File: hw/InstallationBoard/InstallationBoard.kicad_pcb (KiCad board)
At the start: 2 copper layers, 79.5 x 44.9 mm, 24 parts, among them J1 +5V, J10 D4, J11 BRIGHT, J15 GND, J16 GND, J2 GND, J3 CLK, J4 SMS, J5 DW, J6 CL2, J7 D1, J8 D2, J9 D3

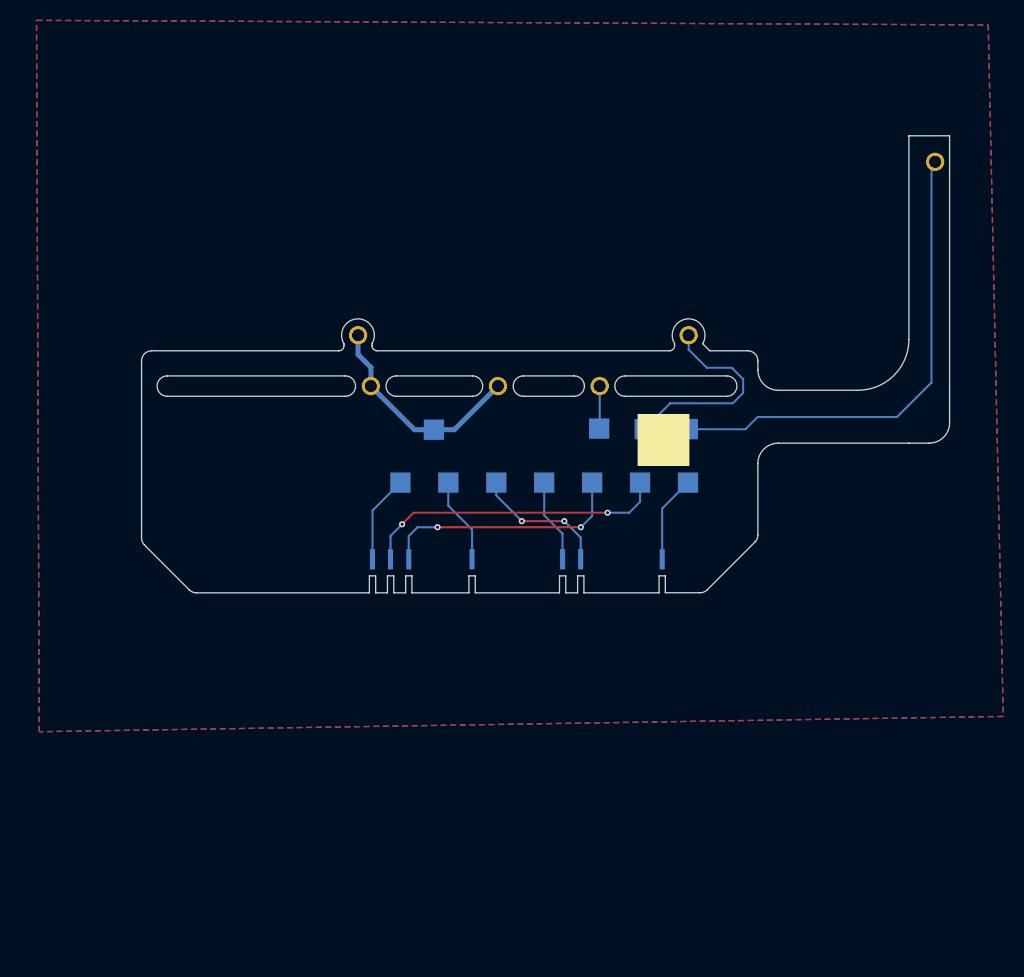
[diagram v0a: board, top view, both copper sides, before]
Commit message: Updated pin assignments on main PCB to match pico code using the correct sequential pins.
54PinTo60RibbonAdapterBoard tweaked trace layout to reduce overall board size slightly.
Added InstallationFlexWithSolderPoints for installing without a ribbon connector.
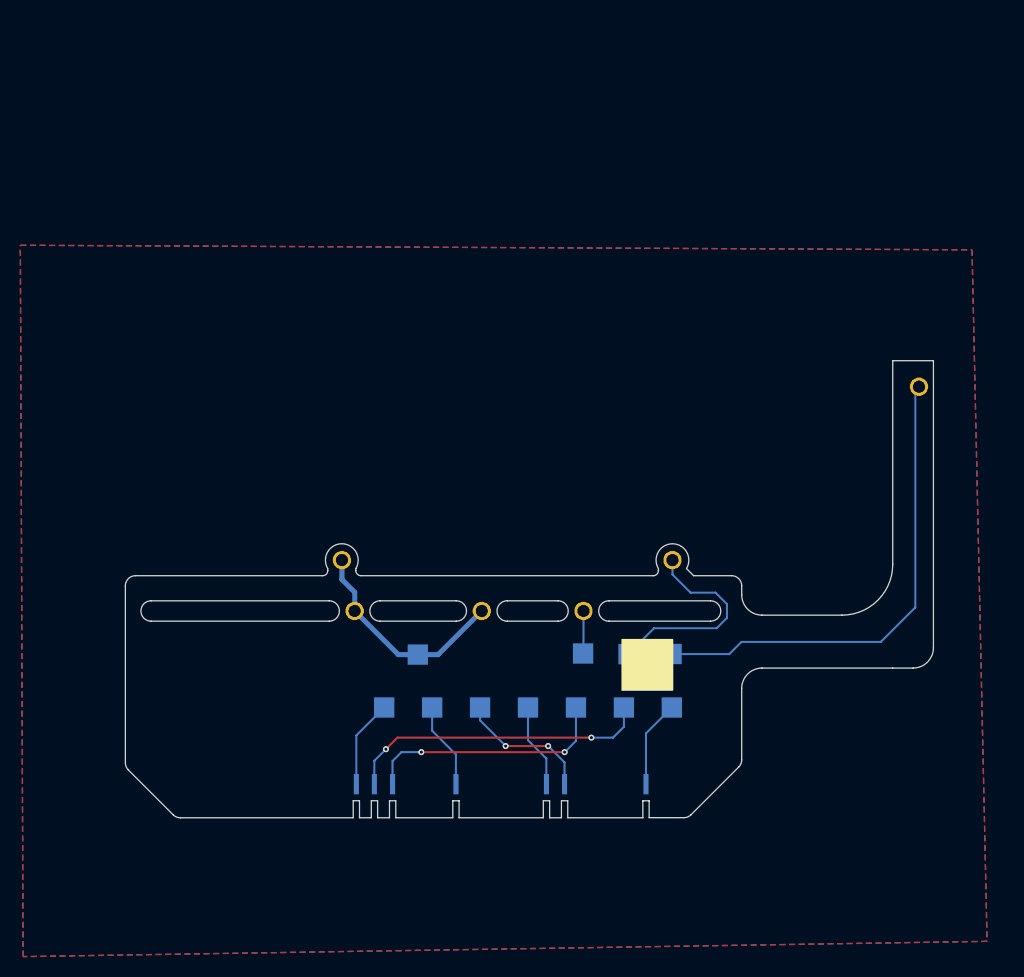
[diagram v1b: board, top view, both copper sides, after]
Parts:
- moved TP10 22.2 mm to (155.0, 133.1)
- moved TP11 22.2 mm to (173.8, 133.1)
- moved TP5 22.2 mm to (145.6, 133.1)
- moved TP6 22.2 mm to (150.3, 133.1)
- moved TP7 22.2 mm to (169.1, 133.1)
- moved TP8 22.2 mm to (164.4, 133.1)
- moved TP9 22.2 mm to (159.7, 133.1)
- moved J1 22.2 mm to (165.2, 123.6)
- moved J10 22.2 mm to (163.3, 140.6)
- moved J11 22.2 mm to (171.3, 140.6)
- moved J15 22.2 mm to (141.4, 118.6)
- moved J16 22.2 mm to (142.7, 123.6)
- moved J2 22.2 mm to (155.2, 123.6)
- moved J3 22.2 mm to (198.1, 101.5)
- moved J4 22.2 mm to (173.9, 118.6)
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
